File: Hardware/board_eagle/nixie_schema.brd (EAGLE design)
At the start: 150 x 170 mm, 230 parts, among them P1 100k, P2 10k, Q1 BC856B, Q3 BC856B, Q4 BCX70H, Q5 NTF5P03, U2 MC7940N, U3 1V5

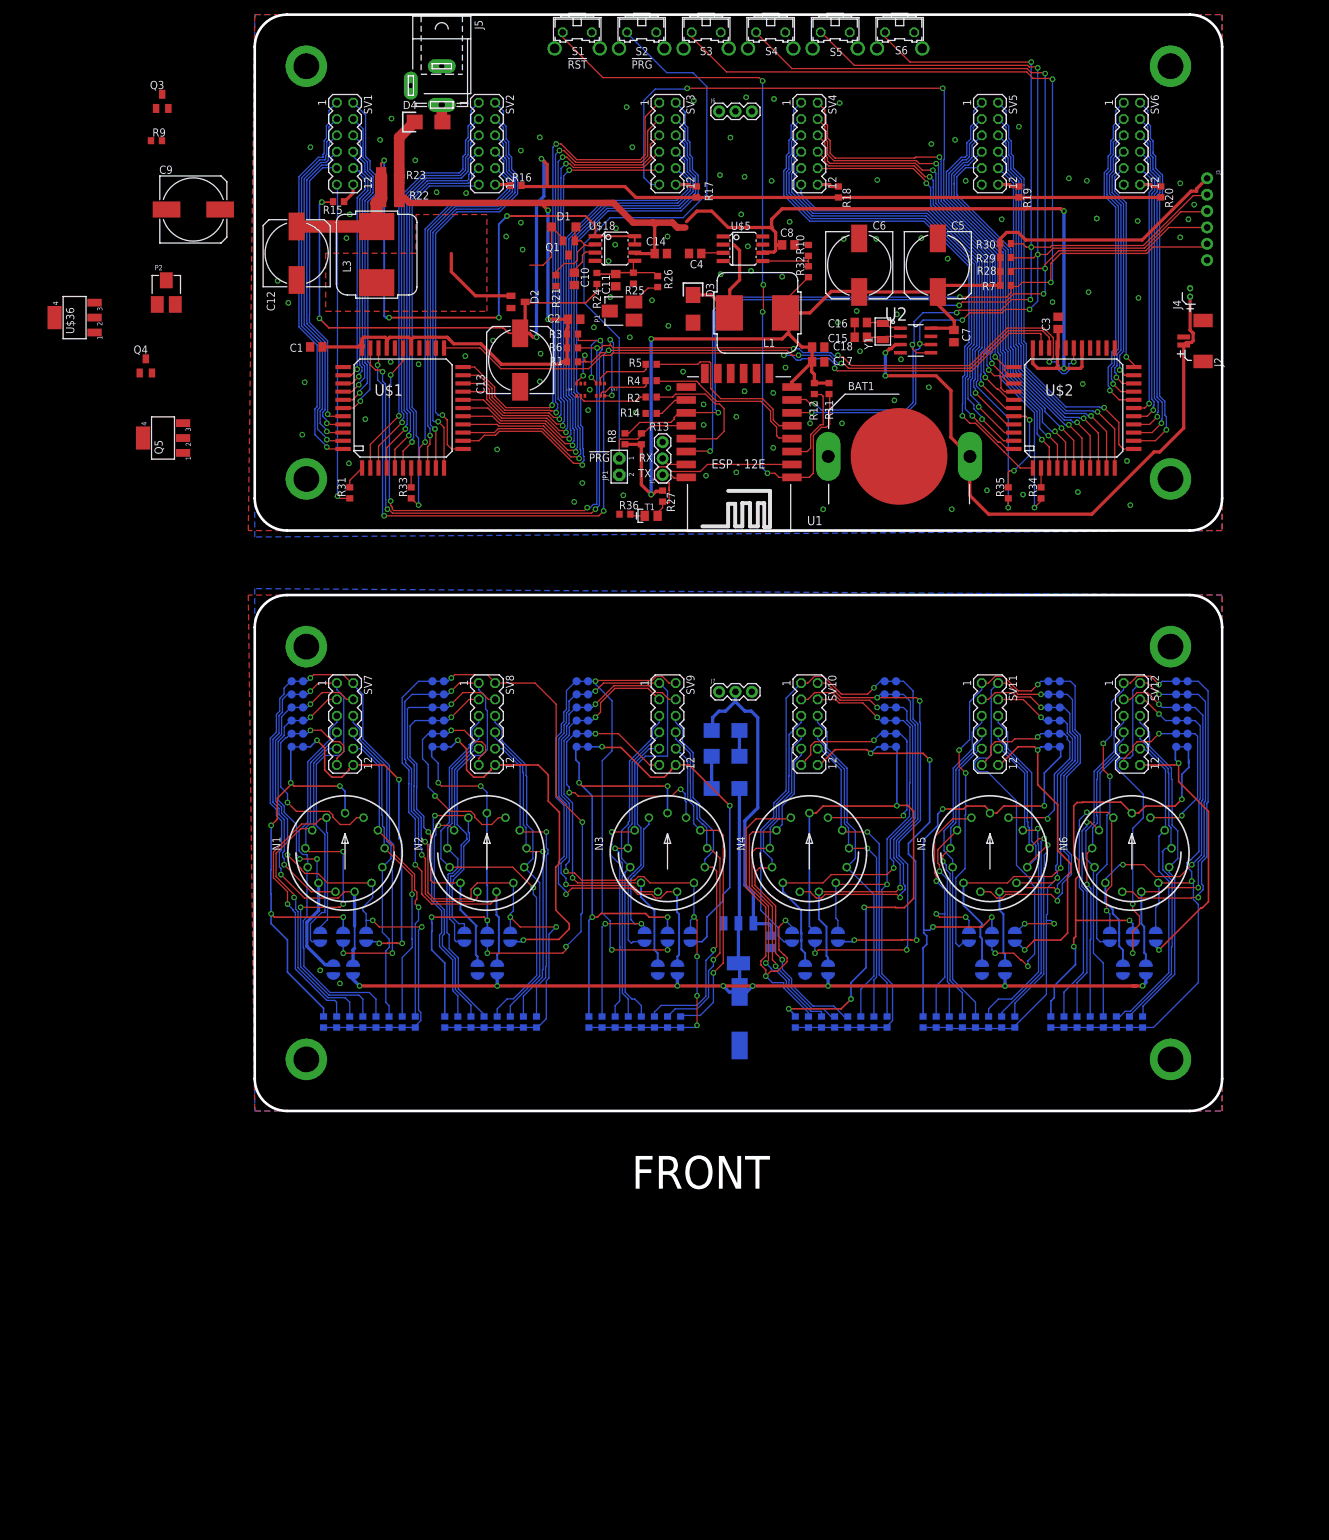
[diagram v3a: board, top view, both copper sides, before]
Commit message: Bottom board routing. Some DRC errors remain.
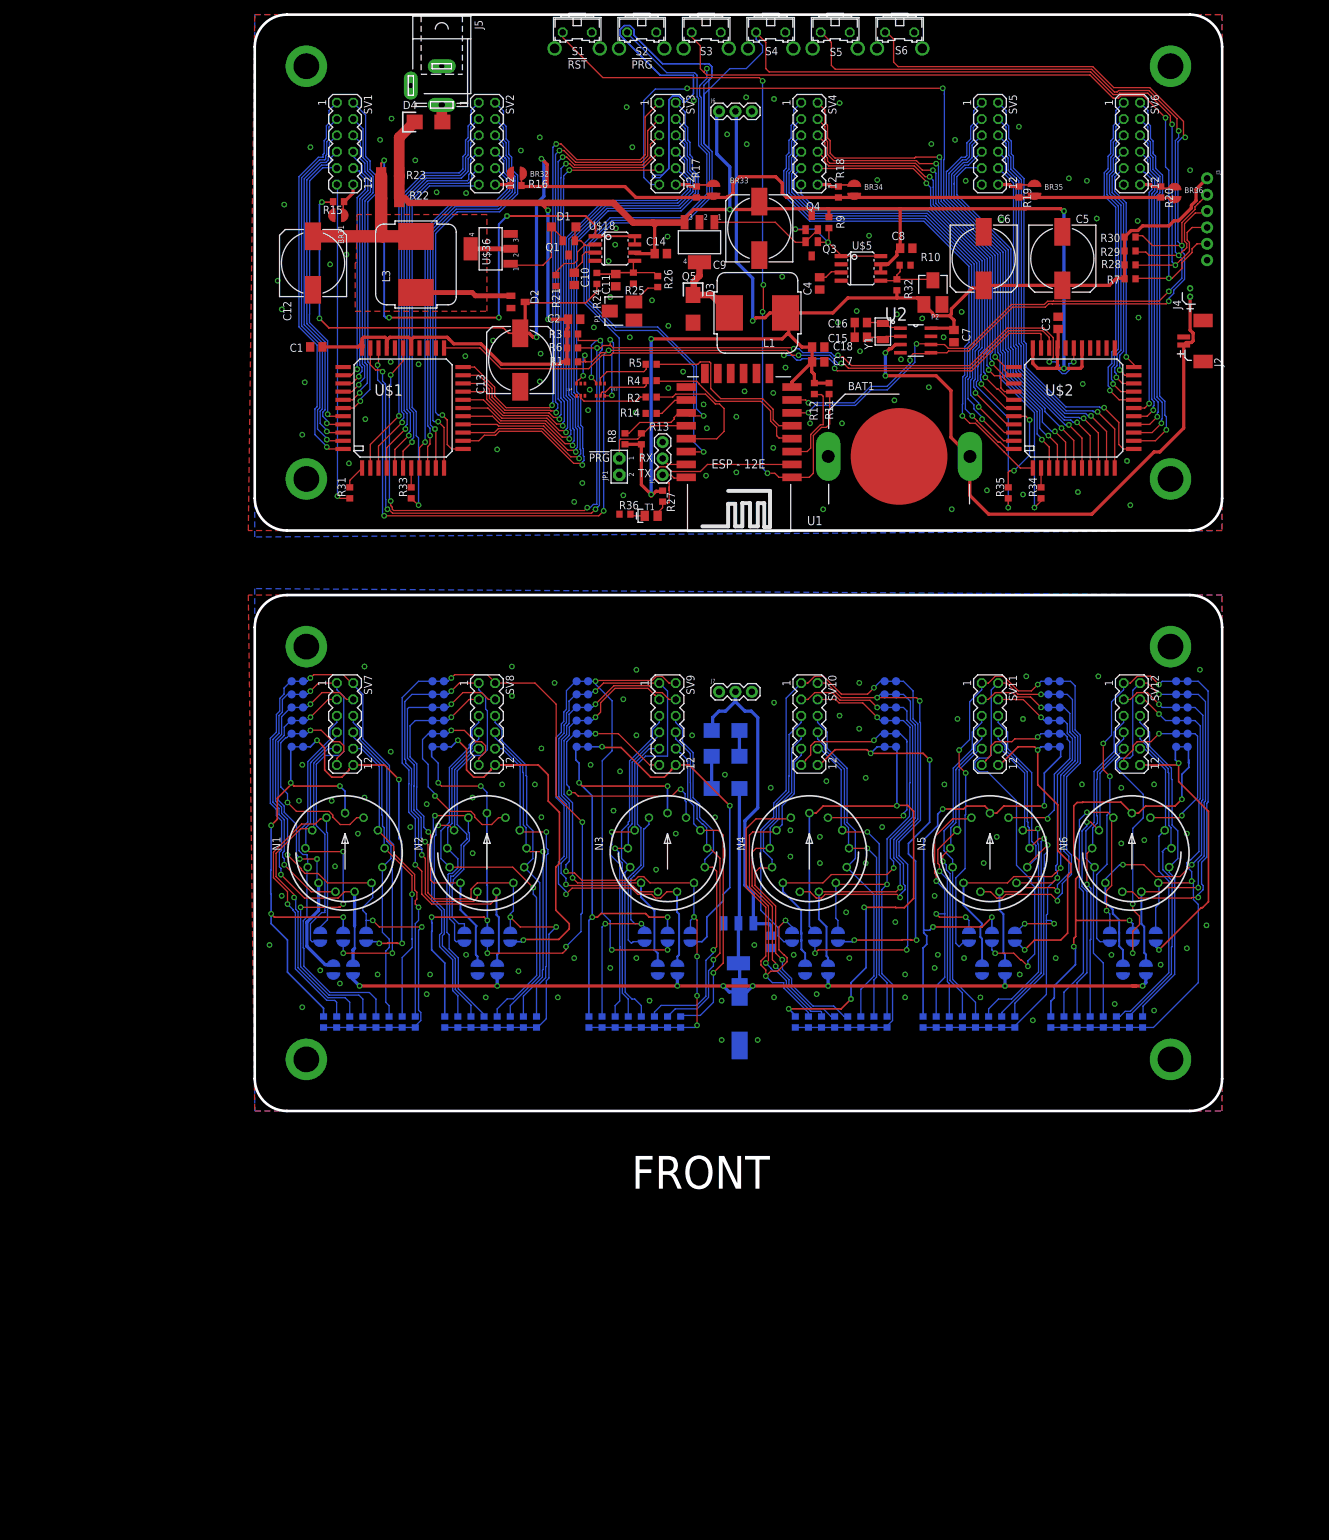
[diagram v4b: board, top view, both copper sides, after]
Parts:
- added BR31, BR32, BR33, BR34, BR35, BR36: HV_SOLDER_BRIDGE, nixe_cmp:HV_SOLDER_BRIDGE
- P2: value 10k -> 100k
- moved P2 118.9 mm to (105.2, 37.0)
- moved Q4 105.6 mm to (86.4, 47.8)
- moved R9 105.0 mm to (89.0, 47.8), turned to 270 degrees
- moved Q3 103.3 mm to (86.4, 43.7), turned to 180 degrees
- moved Q5 88.5 mm to (69.0, 44.7), turned to 180 degrees
- moved C9 87.8 mm to (78.2, 46.9), turned to 90 degrees
- moved U$36 65.4 mm to (36.6, 43.7)
- moved C4 19.9 mm to (87.6, 38.3), turned to 270 degrees
- moved C6 19.3 mm to (113.0, 42.2)
- moved R28 19.3 mm to (135.7, 41.2)
- moved R29 19.3 mm to (135.7, 43.4)
- moved R30 19.3 mm to (135.7, 45.5)
- moved R7 19.3 mm to (135.7, 39.0)
- moved C5 19.3 mm to (125.2, 42.2)
- moved U$5 18.5 mm to (94.0, 40.6)
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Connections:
- net HV_IN+: now also BR31.P$2, BR32.P$2, BR33.P$2, BR34.P$2, BR35.P$2, BR36.P$2
- net N$11: now also BR33.P$1
- net N$8: now also BR34.P$1
- net N$89: now also BR31.P$1
- net N$90: now also BR32.P$1
- net N$91: now also BR36.P$1
- net N$92: now also BR35.P$1
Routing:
- net BUTTON2: track 199.9 -> 351.8 mm, vias 5 -> 3
- net +3V3: track 177.9 -> 209.2 mm, vias 2 -> 3
- net VCC: track 257.9 -> 279.3 mm, vias 4 -> 5
- net N$5: track 0.00 -> 20.6 mm, vias 0 -> 2
- net N$102: track 0.00 -> 18.1 mm
- net BUTTON3: track 160.1 -> 176.9 mm, vias 6 -> 5
- net BUTTON4: track 152.2 -> 167.4 mm, vias 6 -> 5
- net HV_IN+: track 206.1 -> 218.0 mm
- net BUTTON1: track 200.8 -> 211.3 mm
- net V_PULSE: track 13.6 -> 21.1 mm
- net N$13: track 18.2 -> 12.3 mm
- net N$87: track 106.0 -> 109.9 mm
- net N$95: track 11.4 -> 14.5 mm
- net N$11: track 3.36 -> 6.10 mm
- net N$8: track 3.36 -> 5.94 mm
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
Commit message: Most of the board done
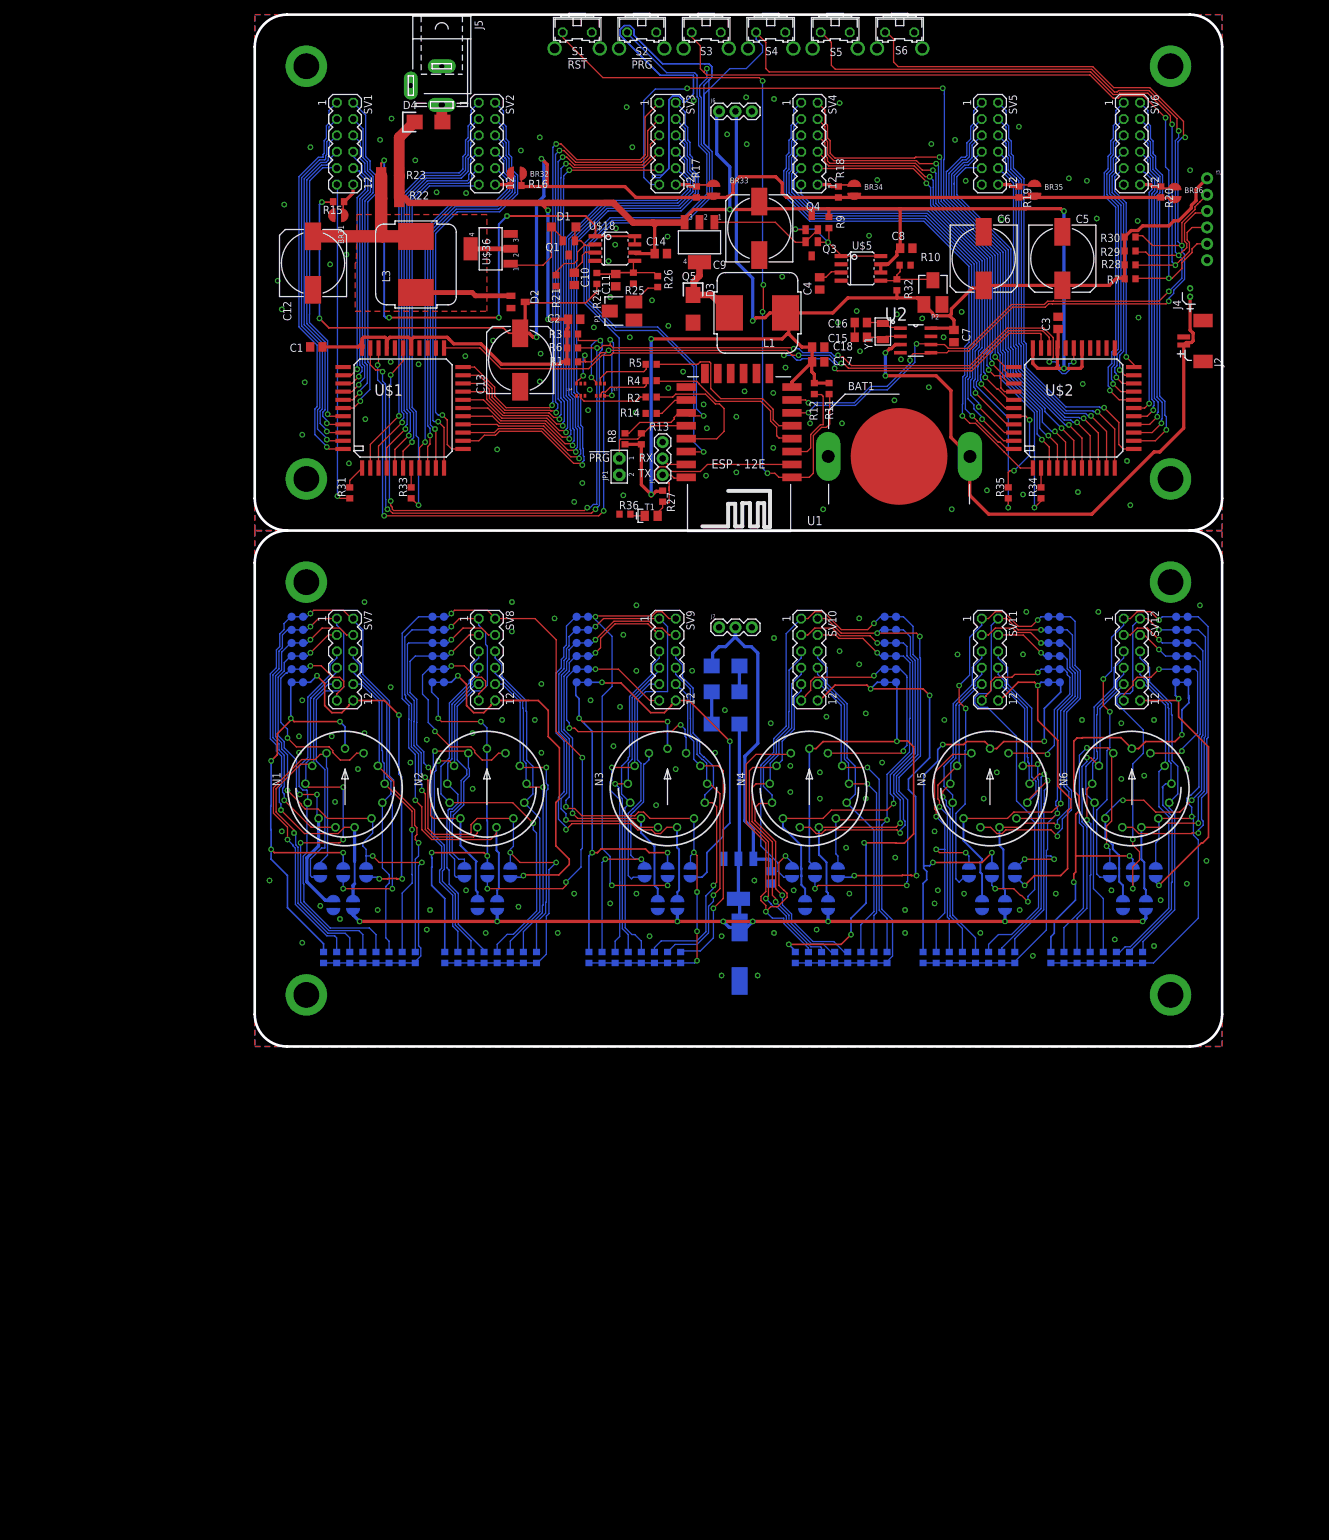
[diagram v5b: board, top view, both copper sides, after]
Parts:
- moved BR1 10.0 mm to (17.3, -53.0)
- moved BR10 10.0 mm to (62.5, -58.1)
- moved BR11 10.0 mm to (65.5, -58.1)
- moved BR12 10.0 mm to (10.2, -53.0)
- moved BR13 10.0 mm to (67.6, -53.0)
- moved BR14 10.0 mm to (64.0, -53.0)
- moved BR15 10.0 mm to (60.5, -53.0)
- moved BR16 10.0 mm to (90.4, -53.0)
- moved BR17 10.0 mm to (86.9, -53.0)
- moved BR18 10.0 mm to (83.3, -53.0)
- moved BR19 10.0 mm to (85.3, -58.1)
- moved BR2 10.0 mm to (15.2, -58.1)
- moved BR20 10.0 mm to (88.9, -58.1)
- moved BR21 10.0 mm to (112.8, -58.1)
- moved BR22 10.0 mm to (116.3, -58.1)
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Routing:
- net 1V5: track 170.8 -> 170.3 mm
- net GND: vias 199 -> 200
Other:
- board size 150 x 170 mm -> 150 x 160 mm
- board text removed: "FRONT"

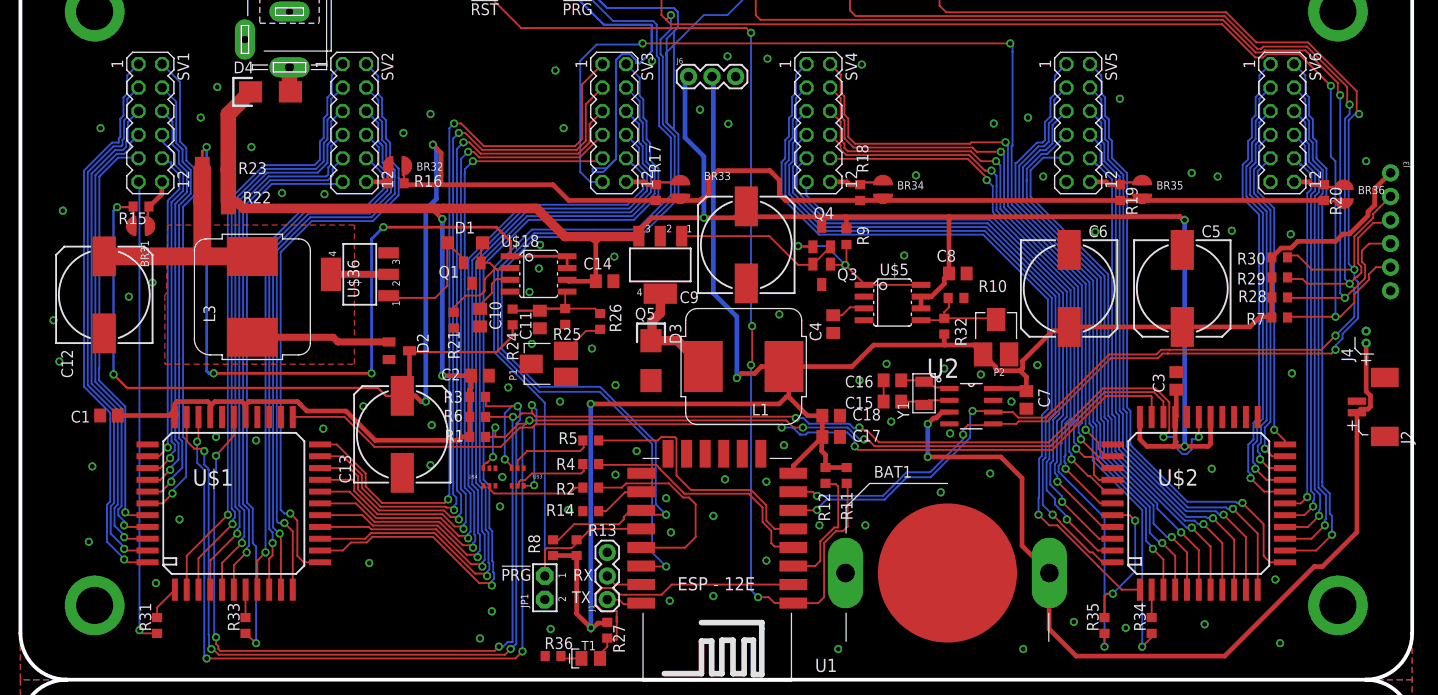
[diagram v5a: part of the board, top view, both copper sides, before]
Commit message: Silk screen touch ups
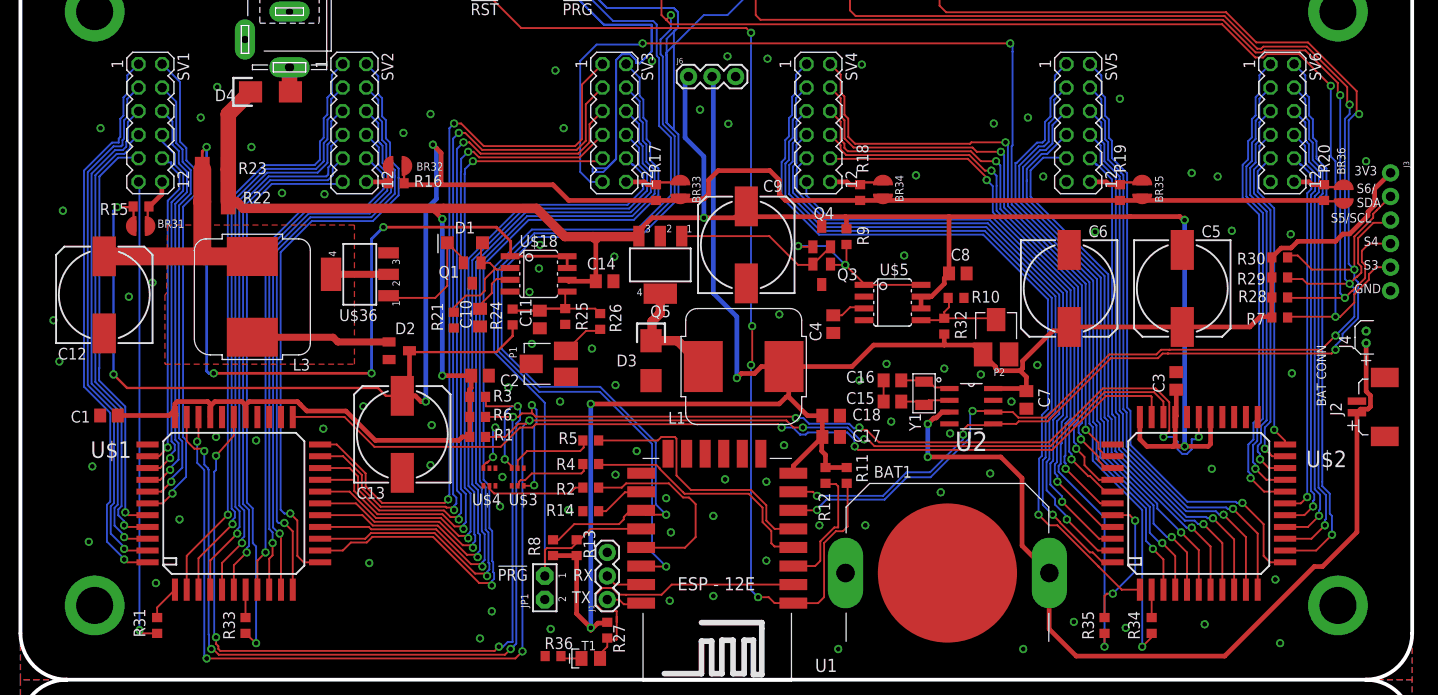
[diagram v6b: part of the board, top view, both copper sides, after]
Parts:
- J2: value (none) -> RTC_CONSMD
- J4: value (none) -> RTC_CONTHT
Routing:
- net HV_MB_8: track 62.8 -> 62.3 mm
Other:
- board text added: "3V3"
- board text added: "BAT CONN"
- board text added: "GND"
- board text added: "S3"
- board text added: "S4"
- board text added: "S5/SCL"
- board text added: "S6/ SDA"
